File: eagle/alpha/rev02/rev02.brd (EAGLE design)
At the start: 100 x 70 mm, 148 parts, among them CN1 HOST, CON1 FX10-80S/8-SV(71), IC1 ICL7660CSA, IC2 ICL7660CSA, Q1 25MHz, Q2 32768, T1 BC847, T2 BC847, T3 BC818, U1 LP3985IM5-3.3, U2 MC74HC1G14DTT1G, U3 ATTINY828R-AU, U4 MC14551BDG, U5 23K640-I/SN, U6 MCP79412-I/SN, Y1 12 MHz +- 30 ppm

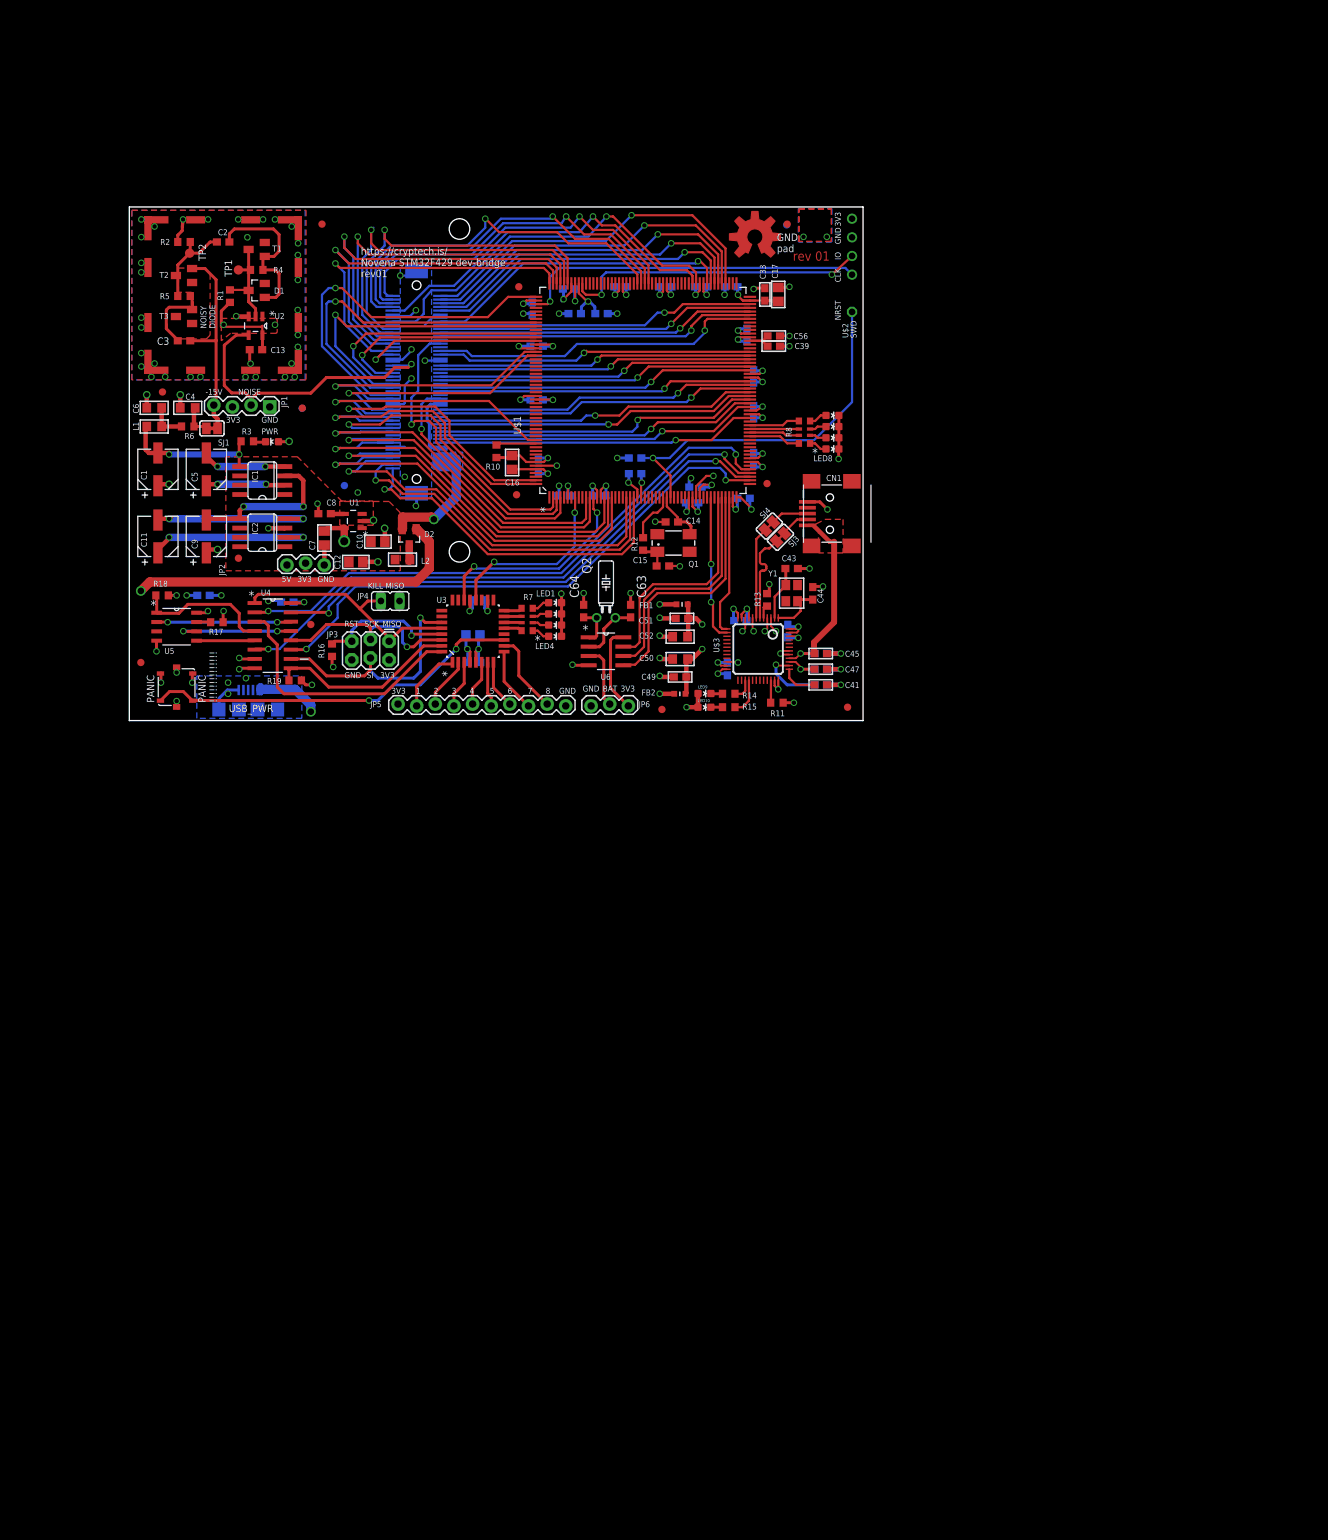
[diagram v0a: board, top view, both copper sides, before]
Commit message: remove components that will not be on the Alpha board
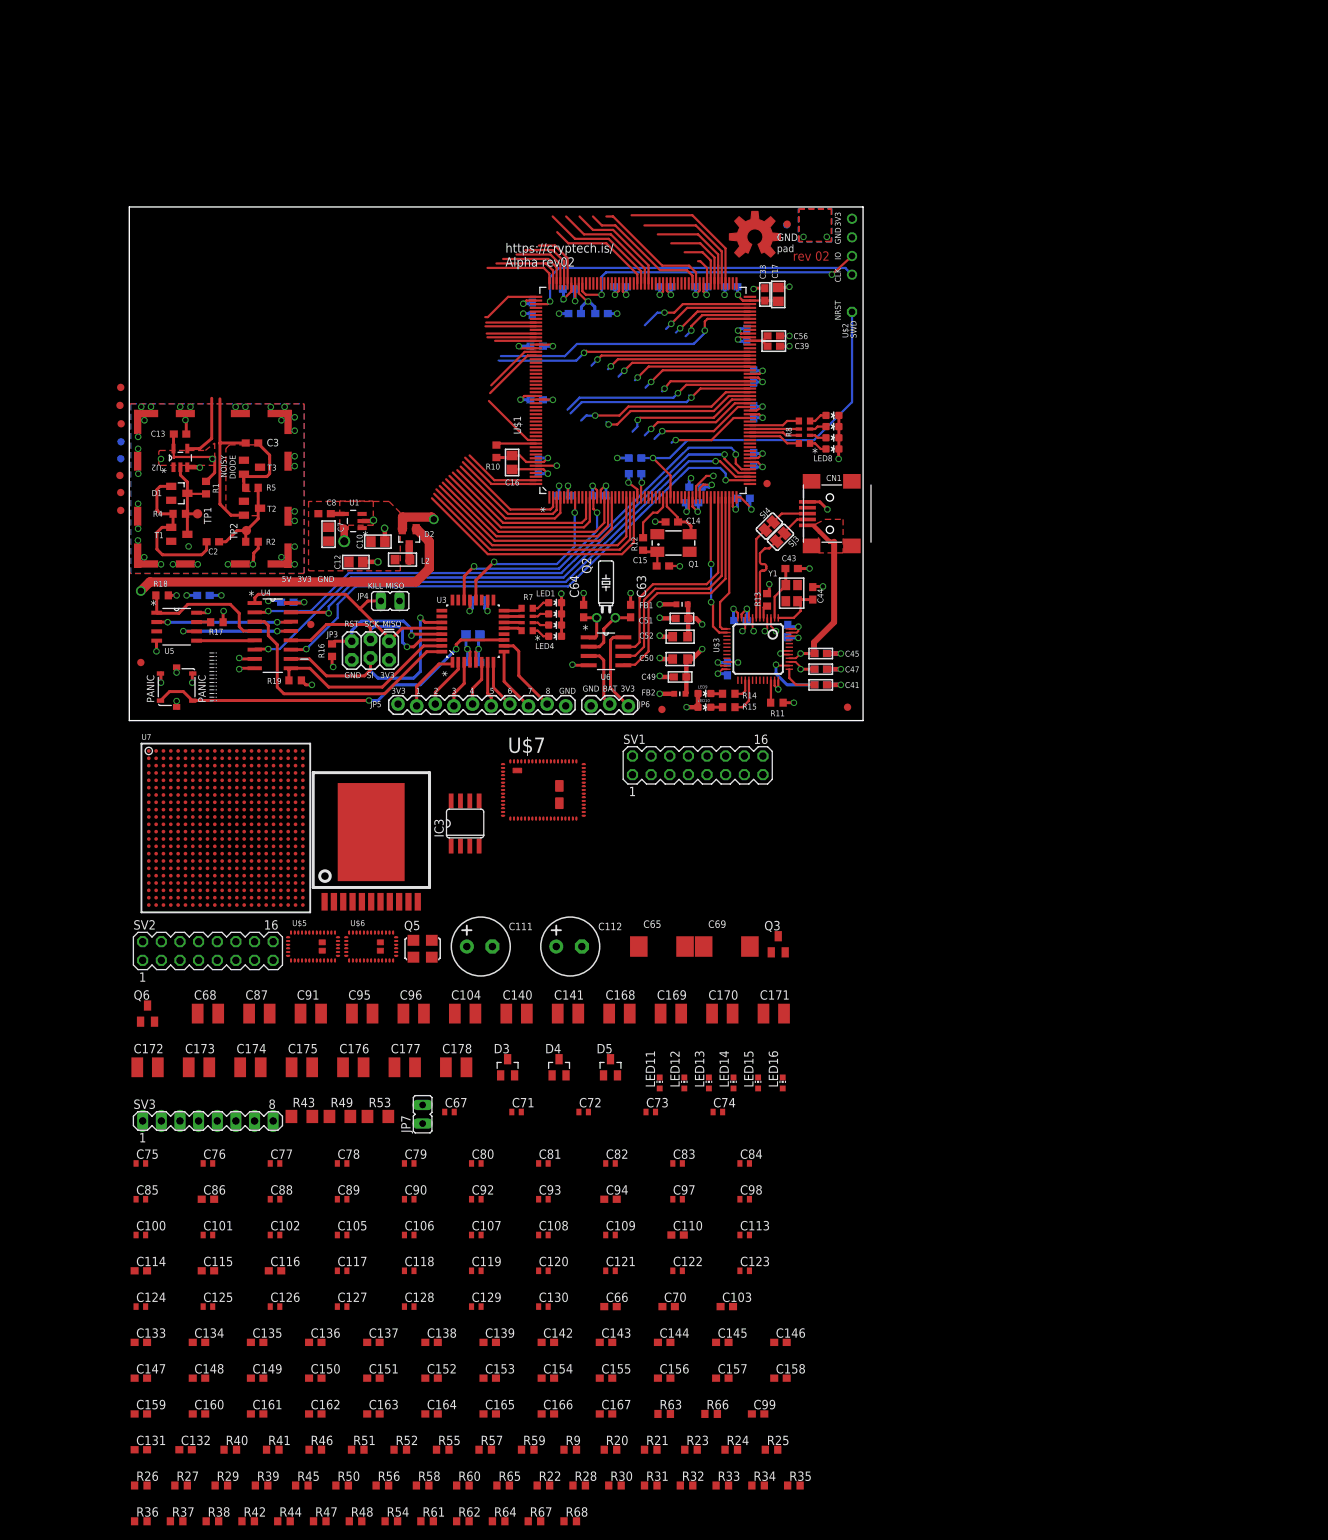
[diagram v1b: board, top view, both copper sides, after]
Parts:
- removed C1, C11, C5, C9: 10uF, UsedComponents:CAPAE530X610N_BIG_PADS
- removed C4, C6: 10 uF X5R 25v, microbuilder:_0805
- removed CON1: FX10-80S/8-SV(71), Novena_FX10A-80S:FX10A-80P/8-SV(71)
- removed IC1, IC2: ICL7660CSA, maxim:SO08
- removed JP1: VOLTS, SparkFun-Connectors:1X04_LOCK
- removed JP2: VCC, SparkFun-Connectors:1X03_LOCK
- removed L1: 10uH, microbuilder:_0805
- removed ORANGE: (no value), UsedComponents:LED-0603
- removed R3: 10K, resistor:R0603
- removed R6: 0, resistor:R0603
- removed SJ1: (no value), microbuilder:SOLDERJUMPER_CLOSEDWIRE@1
- removed USB_PWR: USB-MICROB, SparkFun-Connectors:USB-MICROB
- added C100, C101, C102, C105, C106, C107, C108, C109, C113, C117, C118, C119, C120, C121, C122, C123, C124, C125, C126, C127, C128, C129, C130, C67, C71, C72, C73, C74, C75, C76, C77, C78, C79, C80, C81, C82, C83, C84, C85, C88, C89, C90, C92, C93, C97, C98: 0.47 uF, resistor:C0402
- added C103: 0.47uF, resistor:C0603
- added C104, C140, C141: 10 uF, resistor:C1210
- added C110: 0.01 uF, resistor:C0603
- added C111, C112: 330uF, rc-master:CE-035X080
- added C114, C115, C116, C86, C94: 0.047uF, resistor:C0603
- added C131, C132, C99: 27pF, resistor:C0603
- added C133, C134, C135, C136, C137, C138, C139, C70: 0.1 uF, resistor:C0603
- added C142, C143, C144, C145, C146, C147, C148, C149, C150, C151, C152, C153, C154, C155, C156, C157, C158, C159, C160, C161, C162, C163, C164, C165, C166, C167, C66: 4.7 uF, resistor:C0603
- added C168, C169, C170, C171, C172, C173, C174, C175, C176, C177, C178, C68: 47 uF, resistor:C1210
- added C65, C69: 330 uF, resistor:SMC_D
- added C87, C91, C95, C96: 22 uF, resistor:C1210
- added D3, D4, D5: BAT54, diode:SOT23
- added IC3: N25Q128A13ES, altera-configdevices:SO08
- added JP7: (no value), jumper:JP1
- added LED11, LED12, LED13, LED14, LED15, LED16: (no value), led:CHIP-LED0603
- added Q3, Q6: 2N7002, transistors_gaui:SOT23
- added Q5: ASFL1, crystal:ASF
- added R20, R25, R26, R29, R39, R45, R50, R56, R58, R60, R9: 4.7k, resistor:R0603
- added R21, R23, R24, R27: 1.0k, resistor:R0603
- added R22, R30, R31, R32, R33, R61: 330, resistor:R0603
- added R28, R67, R68: 0, resistor:R0603
- added R34, R54, R62: 100, resistor:R0603
- added R35, R36, R37: 10k, resistor:R0603
- added R38, R44: 62k, resistor:R0603
- added R40, R46: 205k, resistor:R0603
- added R41: 147k, resistor:R0603
- added R42, R48: 470, resistor:R0603
- added R43, R49, R53: 0, resistor:R1206
- added R47: 59k, resistor:R0603
- added R51: 150k, resistor:R0603
- added R52: 226k, resistor:R0603
- added R55, R57, R59: 100k, resistor:R0603
- added R63: 4.64k, resistor:R0603
- added R64: 56k, resistor:R0603
- added R65: 6.3k, resistor:R0603
- added R66: 1.21k, resistor:R0603
- added SV1, SV2: (no value), con-lstb:MA08-2
- added SV3: (no value), con-lstb:MA08-1
- added U$5, U$6: EN6347QI, Alpha-Power:QFN38_4X7X1.85
- added U$7: EN5364QI, Alpha-Power:QFN68_8X11X1.85
- added U$8: LMZ13608, Alpha-Power:NDY
- added U7: XC7A200TFBG484, Xilinx_XC7A200TFBG484:FF484
- moved FID8 62.2 mm to (0.61, 37.5)
- moved FID12 54.0 mm to (0.61, 39.9)
- moved R2 41.9 mm to (18.5, 33.2), turned to 180 degrees
- moved C2 40.9 mm to (13.2, 33.2), turned to 180 degrees
- moved T1 40.2 mm to (8.59, 34.2), turned to 270 degrees
- moved TP2 38.6 mm to (17.7, 34.7), turned to 270 degrees
- moved FID14 35.3 mm to (0.61, 54.3)
- moved R4 34.9 mm to (8.59, 37.0), turned to 0 degrees
- moved TP1 33.7 mm to (11.1, 37.0), turned to 270 degrees
- moved T2 33.0 mm to (18.5, 37.8), turned to 270 degrees
- moved FID5 30.7 mm to (0.62, 44.5)
- moved D1 29.6 mm to (8.59, 39.8), turned to 270 degrees
- moved R5 27.7 mm to (18.5, 40.6), turned to 180 degrees
- moved S1 26.4 mm to (14.4, 40.4), turned to 180 degrees
- moved R1 26.3 mm to (12.2, 40.6), turned to 90 degrees
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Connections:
- removed net MINUS15V: C1.2, IC1.5, L1.1, R3.2
- removed net MINUS5V: C9.2, IC1.3, IC2.5
- removed net N$1: C5.2, IC1.4
- removed net N$11: C6.1, L1.2, R6.2
- removed net N$2: C11.2, IC2.4
- removed net N$3: C11.1, IC2.2
- removed net N$6: C4.1, R6.1, SJ1.2
- removed net N$7: ORANGE.C, R3.1
- removed net N$9: C5.1, IC1.2
- new net DIGITIZED_NOISE: U7.W19
- new net FPGA_DONE: R34.1
- new net FPGA_DONE_INT: LED15.C, R34.2, U7.G11
- new net FPGA_FMC_A0: U7.Y17
- new net FPGA_FMC_A1: U7.Y16
- new net FPGA_FMC_A10: U7.AA14
- new net FPGA_FMC_A11: U7.W14
- new net FPGA_FMC_A12: U7.Y14
- new net FPGA_FMC_A13: U7.AB11
- new net FPGA_FMC_A14: U7.AB12
- new net FPGA_FMC_A15: U7.AA9
- new net FPGA_FMC_A16: U7.AB10
- new net FPGA_FMC_A17: U7.AA10
- new net FPGA_FMC_A18: U7.AA11
- new net FPGA_FMC_A19: U7.V10
- new net FPGA_FMC_A2: U7.AA16
- new net FPGA_FMC_A20: U7.W10
- new net FPGA_FMC_A21: U7.Y11
- new net FPGA_FMC_A22: U7.Y12
- new net FPGA_FMC_A23: U7.W12
- new net FPGA_FMC_A24: U7.V13
- new net FPGA_FMC_A25: U7.V14
- new net FPGA_FMC_A3: U7.AB16
- new net FPGA_FMC_A4: U7.AB17
- new net FPGA_FMC_A5: U7.AA13
- new net FPGA_FMC_A6: U7.AB13
- new net FPGA_FMC_A7: U7.AA15
- new net FPGA_FMC_A8: U7.AB15
- new net FPGA_FMC_A9: U7.Y13
- new net FPGA_FMC_CLK: U7.W11
- new net FPGA_FMC_D0: U7.T3
- new net FPGA_FMC_D1: U7.T1
- new net FPGA_FMC_D10: U7.Y1
- new net FPGA_FMC_D11: U7.U3
- new net FPGA_FMC_D12: U7.V3
- new net FPGA_FMC_D13: U7.AA1
- new net FPGA_FMC_D14: U7.AB1
- new net FPGA_FMC_D15: U7.AB3
- new net FPGA_FMC_D16: U7.AB2
- new net FPGA_FMC_D17: U7.Y3
- new net FPGA_FMC_D18: U7.AA3
- new net FPGA_FMC_D19: U7.AA5
- new net FPGA_FMC_D2: U7.U1
- new net FPGA_FMC_D20: U7.AB5
- new net FPGA_FMC_D21: U7.Y4
- new net FPGA_FMC_D22: U7.AA4
- new net FPGA_FMC_D23: U7.V4
- new net FPGA_FMC_D24: U7.W4
- new net FPGA_FMC_D25: U7.R4
- new net FPGA_FMC_D26: U7.T4
- new net FPGA_FMC_D27: U7.T5
- new net FPGA_FMC_D28: U7.U5
- new net FPGA_FMC_D29: U7.W6
- new net FPGA_FMC_D3: U7.U2
- new net FPGA_FMC_D30: U7.W5
- new net FPGA_FMC_D31: U7.U6
- new net FPGA_FMC_D4: U7.V2
- new net FPGA_FMC_D5: U7.R3
- new net FPGA_FMC_D6: U7.R2
- new net FPGA_FMC_D7: U7.W2
- new net FPGA_FMC_D8: U7.Y2
- new net FPGA_FMC_D9: U7.W1
- new net FPGA_FMC_NE1: U7.V5
- new net FPGA_FMC_NL: U7.R6
- new net FPGA_FMC_NOE: U7.T6
- new net FPGA_FMC_NWAIT: U7.Y6
- new net FPGA_FMC_NWE: U7.AA6
- new net FPGA_GCLK: Q5.3, U7.D17
- new net FPGA_GPIO_A_0: SV1.7, U7.C15
- new net FPGA_GPIO_A_1: SV1.8, U7.E13
- new net FPGA_GPIO_A_2: SV1.9, U7.E14
- new net FPGA_GPIO_A_3: SV1.10, U7.E16
- new net FPGA_GPIO_A_4: SV1.13, U7.D16
- new net FPGA_GPIO_A_5: SV1.14, U7.D14
- new net FPGA_GPIO_A_6: SV1.15, U7.D15
- new net FPGA_GPIO_A_7: SV1.16, U7.B15
- new net FPGA_GPIO_B_0: SV2.7, U7.B16
- new net FPGA_GPIO_B_1: SV2.8, U7.C13
- new net FPGA_GPIO_B_2: SV2.9, U7.B13
- new net FPGA_GPIO_B_3: SV2.10, U7.A15
- new net FPGA_GPIO_B_4: SV2.13, U7.A16
- new net FPGA_GPIO_B_5: SV2.14, U7.A13
- new net FPGA_GPIO_B_6: SV2.15, U7.A14
- new net FPGA_GPIO_B_7: SV2.16, U7.B17
- new net FPGA_GPIO_LED_0: R22.2, U7.T20
- new net FPGA_GPIO_LED_1: R30.2, U7.W21
- new net FPGA_GPIO_LED_2: R31.2, U7.W22
- new net FPGA_GPIO_LED_3: R32.2, U7.AA20
- new net FPGA_GPIO_TAMPER_0: U7.F15
- new net FPGA_GPIO_TAMPER_1: U7.F13
- new net FPGA_INIT_B: Q6.1, R29.2
- new net FPGA_INIT_B_INT: Q6.3, R26.1, U7.U12
- new net FPGA_IRQ_N_0: U7.F14
- new net FPGA_IRQ_N_1: U7.F16
- new net FPGA_IRQ_N_2: U7.E17
- new net FPGA_IRQ_N_3: U7.C14
- new net FPGA_JTAG_TCK: R37.1, SV3.2, U7.V12
- new net FPGA_JTAG_TDI: R35.1, SV3.4, U7.R13
- new net FPGA_JTAG_TDO: SV3.5, U7.U13
- new net FPGA_JTAG_TMS: R36.1, SV3.3, U7.T13
- new net FPGA_M0: R24.1, U7.U11
- new net FPGA_M1: R23.2, U7.U10
- new net FPGA_M2: R21.2, U7.U9
- new net FPGA_MKM_CS_N: U7.T21
- new net FPGA_MKM_MISO: U7.R19
- new net FPGA_MKM_MOSI: U7.P19
- new net FPGA_MKM_SCLK: U7.U21
- new net FPGA_PROGRAM_B: R25.1, U7.N12
- new net FPGA_PROM_CS_B: U7.T19
- new net FPGA_PROM_CS_N: IC3.1, R9.1
- new net FPGA_PROM_MISO: IC3.2, U7.R22
- new net FPGA_PROM_MOSI: IC3.5, U7.P22
- new net FPGA_PROM_SCLK: IC3.6, U7.L12
- new net FPGA_PROM_W_N: IC3.3, JP7.1, R20.2
- new net FPGA_VCCAUX_1V8: C153.1, C154.1, C155.1, C169.1, C70.1, C88.1, C89.1, C90.1, C92.1, C93.1, R43.2, U7.H12, U7.K10, U7.K12, U7.M12, U7.P12, U7.R11
- new net FPGA_VCCINT_1V0: C130.1, C142.1, C143.1, C144.1, C145.1, C146.1, C147.1, C148.1, C149.1, C150.1, C151.1, C152.1, C168.1, C65.+, C66.1, C67.1, C68.1, C69.+, C71.1, C72.1, C73.1, C74.1, C75.1, C76.1, C77.1, C78.1, C79.1, C80.1, C81.1, C82.1, C83.1, C84.1, C85.1, R53.2, U7.H10, U7.H8, U7.J11, U7.J7, U7.J9, U7.K8, U7.L11, U7.L7, U7.M8, U7.N11, U7.N7, U7.P10, U7.P8, U7.R7, U7.R9, U7.T10, U7.T8
- new net FPGA_VCCO_3V3: C100.1, C101.1, C102.1, C105.1, C106.1, C107.1, C108.1, C109.1, C110.1, C113.1, C117.1, C118.1, C119.1, C120.1, C121.1, C122.1, C123.1, C124.1, C125.1, C126.1, C127.1, C128.1, C129.1, C133.1, C134.1, C135.1, C136.1, C156.1, C157.1, C158.1, C159.1, C160.1, C161.1, C162.1, C163.1, C164.1, C165.1, C166.1, C167.1, C170.1, C171.1, C172.1, C173.1, C97.1, C98.1, IC3.7, IC3.8, JP7.2, Q5.4, R25.2, R26.2, R27.2, R28.2, R33.2, R35.2, R36.2, R37.2, R49.2, R9.2, SV1.1, SV1.2, SV1.3, SV1.4, SV2.1, SV2.2, SV2.3, SV2.4, SV3.1, U7.A17, U7.AA17, U7.AA7, U7.AB14, U7.AB4, U7.B14, U7.C1, U7.C21, U7.D18, U7.E15, U7.F12, U7.F2, U7.F22, U7.G19, U7.H16, U7.H6, U7.J13, U7.J3, U7.K20, U7.L17, U7.M14, U7.M4, U7.N1, U7.N21, U7.P18, U7.R15, U7.R5, U7.T12, U7.T2, U7.T22, U7.U19, U7.U8, U7.V16, U7.V6, U7.W13, U7.W3, U7.Y10, U7.Y20
- new net N$27: LED11.A, R22.1
- new net N$28: LED12.A, R30.1
- new net N$29: LED13.A, R31.1
- new net N$30: LED14.A, R32.1
- new net N$32: R27.1, U7.U22
- new net N$33: Q5.1, R28.1
- new net N$34: LED15.A, R33.1
- new net N$35: C115.1, U$5.P$30
- new net N$36: R38.2, U$5.P$29
- new net N$37: R39.1, U$5.P$26
- new net N$38: C132.1, C174.1, R40.2, R42.2, R43.1, U$5.P$10, U$5.P$11, U$5.P$5, U$5.P$6, U$5.P$7, U$5.P$8, U$5.P$9
- new net N$39: C132.2, R40.1, R41.2, U$5.P$31
- new net N$40: C116.1, U$6.P$30
- new net N$41: R44.2, U$6.P$29
- new net N$42: R45.1, U$6.P$26
- new net N$43: C131.1, C175.1, R46.2, R48.2, R49.1, U$6.P$10, U$6.P$11, U$6.P$5, U$6.P$6, U$6.P$7, U$6.P$8, U$6.P$9
- new net N$44: C131.2, R46.1, R47.2, U$6.P$31
- new net N$45: C94.1, U$7.P$59
- new net N$46: R50.1, U$7.P$51
- new net N$47: R67.1, U$7.P$63
- new net N$48: C176.1, C177.1, C99.1, R51.2, R53.1, R54.2, R67.2, U$7.P$10, U$7.P$11, U$7.P$12, U$7.P$13, U$7.P$5, U$7.P$6, U$7.P$7, U$7.P$8, U$7.P$9
- new net N$49: C99.2, R51.1, R52.2, U$7.P$56
- new net N$50: LED16.C, Q3.3
- new net N$51: LED16.A, R61.1
- new net N$52: C103.1, U$8.P$9
- new net N$53: R68.2, U$8.P$3
- new net N$54: R62.1, R63.2, R64.1
- new net N$55: R62.2, U$8.P$4
- new net N$56: R65.1, R66.2, U$8.P$7
- new net POK_VCCAUX: D5.3, R58.1, R59.1, U$5.P$28
- new net POK_VCCINT: D4.3, R56.1, R57.1, U$7.P$54
- new net POK_VCCO: Q3.1, R60.1, U$6.P$28
- new net PWR_18V: C104.1, C140.1, C141.1, C86.1, R64.2, U$8.P$1, U$8.P$2
- new net PWR_ENA_VCCAUX: C139.1, D4.1, R57.2, U$5.P$27
- new net PWR_ENA_VCCINT: C137.1, D3.1, R55.2, U$7.P$52
- new net PWR_ENA_VCCO: C138.1, D5.1, R59.2, U$6.P$27
- new net VCC_5V0: C111.+, C112.+, C114.1, C178.1, C87.1, C91.1, C95.1, C96.1, D3.3, R39.2, R45.2, R50.2, R55.1, R56.2, R58.2, R60.2, R61.2, R65.2, U$5.P$19, U$5.P$20, U$5.P$21, U$5.P$33, U$6.P$19, U$6.P$20, U$6.P$21, U$6.P$33, U$7.P$34, U$7.P$35, U$7.P$36, U$7.P$37, U$7.P$38, U$7.P$39, U$7.P$40, U$7.P$41, U$7.P$42, U$7.P$43, U$7.P$53, U$8.P$11, U$8.P$12
- new net VPGA_VCCO_3V3: R24.2
- net 3V3: no longer JP1.3, JP2.2
- net 5V: no longer IC1.8, IC2.8, JP2.3
- net DIGITIZED: no longer CON1.65_F_DX18, JP1.2
- net FMC_A0: no longer CON1.46_F_LVDS7_N
- net FMC_A1: no longer CON1.45_F_DX15
- net FMC_A10: no longer CON1.30_
- net FMC_A11: no longer CON1.29_
- net FMC_A12: no longer CON1.80_
- net FMC_A13: no longer CON1.79_
- net FMC_A14: no longer CON1.78_DDC_SCL
- net FMC_A15: no longer CON1.77_
- net FMC_A16: no longer CON1.4_F_DX11
- net FMC_A17: no longer CON1.5_DDC_SDA
- net FMC_A18: no longer CON1.6_F_LVDS11_P
- net FMC_A19: no longer CON1.50_
- net FMC_A2: no longer CON1.44_F_DX7
- net FMC_A20: no longer CON1.12_F_DX17
- net FMC_A21: no longer CON1.25_F_DX14
- net FMC_A3: no longer CON1.43_F_DX12
- net FMC_A4: no longer CON1.42_FDX_6
- net FMC_A5: no longer CON1.41_F_DX13
- net FMC_A6: no longer CON1.35_
- net FMC_A7: no longer CON1.34_
- net FMC_A8: no longer CON1.33_
- net FMC_A9: no longer CON1.32_
- net FMC_CLK: no longer CON1.62_F_LVDS_CK0_N
- net FMC_D0: no longer CON1.75_
- net FMC_D1: no longer CON1.76_
- net FMC_D10: no longer CON1.17_F_LVDS15_N
- net FMC_D11: no longer CON1.16_F_LVDS15_P
- net FMC_D12: no longer CON1.15_F_LVDSB_P
- net FMC_D13: no longer CON1.1_F_DX0
- net FMC_D14: no longer CON1.2_F_DX3
- net FMC_D15: no longer CON1.3_F_DX2
- net FMC_D16: no longer CON1.14_F_LVDSB_N
- net FMC_D17: no longer CON1.10_F_LVDSC_P
- net FMC_D18: no longer CON1.9_F_LVDSC_N
- net FMC_D19: no longer CON1.8_F_DX1
- net FMC_D2: no longer CON1.59_
- net FMC_D20: no longer CON1.7_F_LVDS11_N
- net FMC_D21: no longer CON1.73_
- net FMC_D22: no longer CON1.72_
- net FMC_D23: no longer CON1.71_
- net FMC_D24: no longer CON1.70_
- net FMC_D25: no longer CON1.69_
- net FMC_D26: no longer CON1.67_
- net FMC_D27: no longer CON1.57_
- net FMC_D28: no longer CON1.53_
- net FMC_D29: no longer CON1.52_
- net FMC_D3: no longer CON1.60_F_LVDS9_P
- net FMC_D30: no longer CON1.49_
- net FMC_D31: no longer CON1.47_F_LVDS7_P
- net FMC_D4: no longer CON1.27_
- net FMC_D5: no longer CON1.26_F_LVDS4_P
- net FMC_D6: no longer CON1.23_F_LVDS_CK1_N
- net FMC_D7: no longer CON1.22_F_LVDS_CK1_P
- net FMC_D8: no longer CON1.20_F_LVDS0_N
- net FMC_D9: no longer CON1.19_F_LVDS0_P
- net FMC_NE1: no longer CON1.55_
- net FMC_NL: no longer CON1.54_
- net FMC_NOE: no longer CON1.63_F_LVDS_CK0_P
- net FMC_NWAIT: no longer CON1.56_
- net FMC_NWE: no longer CON1.66_
- net GND: now also C100.2, C101.2, C102.2, C103.2, C104.2, C105.2, C106.2, C107.2, C108.2, C109.2, C110.2, C111.-, C112.-, C113.2, C114.2, C115.2, C116.2, C117.2, C118.2, C119.2, C120.2, C121.2, C122.2, C123.2, C124.2, C125.2, C126.2, C127.2, C128.2, C129.2, C130.2, C133.2, C134.2, C135.2, C136.2, C137.2, C138.2, C139.2, C140.2, C141.2, C142.2, C143.2, C144.2, C145.2, C146.2, C147.2, C148.2, C149.2, C150.2, C151.2, C152.2, C153.2, C154.2, C155.2, C156.2, C157.2, C158.2, C159.2, C160.2, C161.2, C162.2, C163.2, C164.2, C165.2, C166.2, C167.2, C168.2, C169.2, C170.2, C171.2, C172.2, C173.2, C174.2, C175.2, C176.2, C177.2, C178.2, C65.-, C66.2, C67.2, C68.2, C69.-, C70.2, C71.2, C72.2, C73.2, C74.2, C75.2, C76.2, C77.2, C78.2, C79.2, C80.2, C81.2, C82.2, C83.2, C84.2, C85.2, C86.2, C87.2, C88.2, C89.2, C90.2, C91.2, C92.2, C93.2, C94.2, C95.2, C96.2, C97.2, C98.2, IC3.4, LED11.C, LED12.C, LED13.C, LED14.C, Q3.2, Q5.2, Q6.2, R20.1, R21.1, R23.1, R29.1, R38.1, R41.1, R42.1, R44.1, R47.1, R48.1, R52.1, R54.1, R63.1, R66.1, R68.1, SV1.11, SV1.12, SV1.5, SV1.6, SV2.11, SV2.12, SV2.5, SV2.6, SV3.6, SV3.7, SV3.8, U$5.P$13, U$5.P$14, U$5.P$15, U$5.P$16, U$5.P$17, U$5.P$18, U$5.P$32, U$5.P$39, U$5.P$40, U$6.P$13, U$6.P$14, U$6.P$15, U$6.P$16, U$6.P$17, U$6.P$18, U$6.P$32, U$6.P$39, U$6.P$40, U$7.P$1, U$7.P$2, U$7.P$27, U$7.P$28, U$7.P$29, U$7.P$3, U$7.P$30, U$7.P$31, U$7.P$32, U$7.P$33, U$7.P$4, U$7.P$55, U$7.P$64, U$7.P$65, U$7.P$66, U$7.P$67, U$7.P$68, U$7.P$69, U$7.P$70, U$7.P$71, U$8.P$5, U$8.P$6, U$8.P$8, U7.A11, U7.A12, U7.A2, U7.A22, U7.A3, U7.A5, U7.A7, U7.A9, U7.AA12, U7.AA2, U7.AA22, U7.AB19, U7.AB9, U7.B12, U7.B19, U7.B3, U7.C10, U7.C12, U7.C16, U7.C3, U7.C6, U7.D12, U7.D13, U7.D3, U7.D4, U7.D8, U7.E11, U7.E12, U7.E20, U7.E4, U7.E5, U7.E7, U7.E9, U7.F11, U7.F17, U7.F5, U7.G10, U7.G12, U7.G14, U7.G5, U7.G6, U7.G7, U7.G8, U7.G9, U7.H1, U7.H11, U7.H21, U7.H7, U7.H9, U7.J10, U7.J12, U7.J18, U7.J8, U7.K11, U7.K15, U7.K5, U7.K7, U7.K9, U7.L2, U7.L22, U7.L8, U7.L9, U7.M10, U7.M11, U7.M19, U7.M7, U7.N10, U7.N16, U7.N6, U7.N8, U7.N9, U7.P11, U7.P13, U7.P3, U7.P7, U7.P9, U7.R10, U7.R12, U7.R20, U7.R8, U7.T11, U7.T17, U7.T7, U7.T9, U7.U14, U7.U4, U7.V1, U7.V11, U7.V21, U7.W18, U7.W8, U7.Y15, U7.Y5; no longer C1.1, C4.2, C6.2, C9.1, CON1.GND1, CON1.GND2, CON1.GND3, CON1.GND4, CON1.GND5, CON1.GND6, CON1.GND7, CON1.GND8, CON1.GUIDE@L, CON1.GUIDE@R, IC2.3, JP1.1, JP2.1, ORANGE.A, USB_PWR.GND, USB_PWR.MT1, USB_PWR.MT2
- net MINUS15V_STABLE: no longer JP1.4, SJ1.1
- net P-5.0V_MAIN: no longer CON1.36_P-5.0V_MAIN, CON1.37_P-5.0V_MAIN, CON1.38_P-5.0V_MAIN, CON1.39_P-5.0V_MAIN, CON1.40_P-5.0V_MAIN
- net USB_PWR_VBUS: no longer USB_PWR.VBUS
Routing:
- net GND: track 224.8 -> 172.4 mm, vias 83 -> 65
- net FMC_D27: track 51.7 -> 8.05 mm, vias 1 -> 0
- net FMC_D24: track 52.1 -> 9.95 mm, vias 1 -> 0
- net FMC_D22: track 49.8 -> 8.90 mm, vias 1 -> 0
- net FMC_D25: track 50.3 -> 9.88 mm, vias 1 -> 0
- net FMC_D2: track 46.8 -> 6.78 mm, vias 1 -> 0
- net FMC_D23: track 49.1 -> 9.12 mm, vias 1 -> 0
- net FMC_D21: track 47.4 -> 8.06 mm, vias 1 -> 0
- net FMC_A18: track 42.2 -> 3.71 mm, vias 1 -> 0
- net FMC_D26: track 47.9 -> 10.1 mm, vias 1 -> 0
- net FMC_A15: track 52.1 -> 14.6 mm, vias 1 -> 0
- net FMC_A17: track 43.7 -> 7.15 mm, vias 1 -> 0
- net FMC_D0: track 53.2 -> 16.9 mm, vias 1 -> 0
- net FMC_D3: track 42.2 -> 6.88 mm, vias 1 -> 0
- net FMC_A16: track 45.3 -> 10.2 mm, vias 1 -> 0
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- removed copper zone on layer 16, net P-5.0V_MAIN
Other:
- board text added: "https://cryptech.is/ Alpha rev02"
- board text added: "rev 02"
- board text removed: "-15V"
- board text removed: "NOISE"
- board text removed: "PWR"
- board text removed: "https://cryptech.is/ Novena STM32F429 dev-bridge rev01"
- board text removed: "rev 01"
